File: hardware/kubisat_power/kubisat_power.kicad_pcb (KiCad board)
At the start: 2 copper layers, 21 parts, among them U1 TPS79601DCQ, U2 INA3221

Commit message: complete schematic, todo add solar connectors
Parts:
- added BT1: 1048P, 1048P:BAT_1048P, F.Cu at (171.5, 88.1)
- added C10: 22u, Capacitor_SMD:C_1206_3216Metric, F.Cu at (190.2, 117.8)
- added C11: 100n, Capacitor_SMD:C_0805_2012Metric, F.Cu at (157.6, 110.3)
- added C12: 10u, Capacitor_SMD:C_0805_2012Metric, F.Cu at (157.6, 113.3)
- added C13: 100n, Capacitor_SMD:C_0805_2012Metric, F.Cu at (157.6, 116.3)
- added C14: 47/50V, Capacitor_SMD:C_Elec_6.3x5.8, F.Cu at (150.4, 112.8)
- added C15: 10u, Capacitor_SMD:C_0805_2012Metric, F.Cu at (157.6, 119.3)
- added C16: 10u/25V, Capacitor_SMD:C_1210_3225Metric, F.Cu at (190.2, 121.6)
- added C17: 220n, Capacitor_SMD:C_0805_2012Metric, F.Cu at (157.6, 122.3)
- added C9: 10u, Capacitor_SMD:C_1206_3216Metric, F.Cu at (190.2, 114.5)
- added D1: SS14, Diode_SMD:D_SMA, F.Cu at (197.8, 111.0)
- added D10: PV, LED_SMD:LED_0805_2012Metric, F.Cu at (180.0, 113.3)
- added D11: 5V_OK, LED_SMD:LED_0805_2012Metric, F.Cu at (180.0, 116.3)
- added D2: U_CHG, LED_SMD:LED_0805_2012Metric, F.Cu at (171.1, 110.3)
- added D3: U_DONE, LED_SMD:LED_0805_2012Metric, F.Cu at (171.1, 113.3)
- added D4: S_DONE, LED_SMD:LED_0805_2012Metric, F.Cu at (171.1, 116.3)
- added D5: S_CHG, LED_SMD:LED_0805_2012Metric, F.Cu at (175.6, 110.3)
- added D6: SS54, Diode_SMD:D_SMA, F.Cu at (197.8, 115.6)
- added D7: TC, LED_SMD:LED_0805_2012Metric, F.Cu at (175.6, 113.3)
- added D8: WARN, LED_SMD:LED_0805_2012Metric, F.Cu at (175.6, 116.3)
- added D9: CRIT, LED_SMD:LED_0805_2012Metric, F.Cu at (180.0, 110.3)
- added J1: USB_C_Receptacle_PowerOnly_6P, Connector_USB:USB_C_Receptacle_HRO_TYPE-C-31-M-17, F.Cu at (174.7, 122.9)
- added JP1: SolderJumper_2_Open, Jumper:SolderJumper-2_P1.3mm_Open_RoundedPad1.0x1.5mm, F.Cu at (189.5, 125.5)
- added L1: 3.3.uH, Inductor_SMD:L_Cenker_CKCS5040, F.Cu at (197.3, 121.2)
- added L2: 100, Inductor_SMD:L_Bourns_SRP7028A_7.3x6.6mm, F.Cu at (150.4, 121.0)
- added Q1: Si2305, Package_TO_SOT_SMD:SOT-23, F.Cu at (211.3, 124.4)
- added R12: 10k, Resistor_SMD:R_0805_2012Metric, F.Cu at (130.0, 110.2)
- added R13: 13k3, Resistor_SMD:R_0805_2012Metric, F.Cu at (130.0, 113.2)
- added R14: 1k5, Resistor_SMD:R_0805_2012Metric, F.Cu at (130.0, 116.1)
- added R15: 1k, Resistor_SMD:R_0805_2012Metric, F.Cu at (130.0, 119.1)
- added R16: 1k, Resistor_SMD:R_0805_2012Metric, F.Cu at (130.0, 122.0)
- added R17: 5k1, Resistor_SMD:R_0805_2012Metric, F.Cu at (130.0, 125.0)
- added R18: 5k1, Resistor_SMD:R_0805_2012Metric, F.Cu at (134.4, 110.2)
- added R19: 1k, Resistor_SMD:R_2512_6332Metric_Pad1.40x3.35mm_HandSolder, F.Cu at (164.3, 111.2)
- added R20: 100, Resistor_SMD:R_2512_6332Metric_Pad1.40x3.35mm_HandSolder, F.Cu at (164.3, 116.1)
- added R21: 27k, Resistor_SMD:R_0805_2012Metric, F.Cu at (134.4, 113.2)
- added R22: 6k8, Resistor_SMD:R_0805_2012Metric, F.Cu at (134.4, 116.1)
- added R23: 1k, Resistor_SMD:R_0805_2012Metric, F.Cu at (134.4, 119.1)
- added R24: 1k, Resistor_SMD:R_0805_2012Metric, F.Cu at (134.4, 122.0)
- added R25: R050, Resistor_SMD:R_2512_6332Metric_Pad1.40x3.35mm_HandSolder, F.Cu at (164.3, 121.0)
- added R26: 120, Resistor_SMD:R_0805_2012Metric, F.Cu at (134.4, 125.0)
- added R27: 10k, Resistor_SMD:R_0805_2012Metric, F.Cu at (138.8, 110.2)
- added R28: 10k, Resistor_SMD:R_0805_2012Metric, F.Cu at (138.8, 113.2)
- added R29: 10k, Resistor_SMD:R_0805_2012Metric, F.Cu at (138.8, 116.1)
- added R30: 10k, Resistor_SMD:R_0805_2012Metric, F.Cu at (138.8, 119.1)
- added R31: 10k, Resistor_SMD:R_0805_2012Metric, F.Cu at (138.8, 122.0)
- added R32: 10k, Resistor_SMD:R_0805_2012Metric, F.Cu at (138.8, 125.0)
- added R33: 1k, Resistor_SMD:R_0805_2012Metric, F.Cu at (143.2, 110.2)
- added R34: 1k, Resistor_SMD:R_0805_2012Metric, F.Cu at (143.2, 113.2)
- added R35: 1k, Resistor_SMD:R_0805_2012Metric, F.Cu at (143.2, 116.1)
- added R36: 1k, Resistor_SMD:R_0805_2012Metric, F.Cu at (143.2, 119.1)
- added R37: 1k, Resistor_SMD:R_0805_2012Metric, F.Cu at (143.2, 122.0)
- added SW1: SW_Wuerth_450301014042, Button_Switch_THT:SW_Slide-03_Wuerth-WS-SLTV_10x2.5x6.4_P2.54mm, F.Cu at (188.0, 110.8)
- added U3: LN2220, Package_TO_SOT_SMD:TSOT-23-6_HandSoldering, F.Cu at (205.3, 124.3)
- added U4: CN3791, Package_SO:SSOP-10-1EP_3.9x4.9mm_P1mm_EP2.1x3.3mm, F.Cu at (206.1, 112.2)
- added U5: TP4056, Package_SO:SOIC-8-1EP_3.9x4.9mm_P1.27mm_EP2.29x3mm, F.Cu at (206.1, 118.8)
- added U6: DW01A, Package_TO_SOT_SMD:SOT-23-6, F.Cu at (184.8, 115.2)
- added U7: FS8205, Package_TO_SOT_SMD:SOT-23-6, F.Cu at (184.8, 119.8)
- R11, R5, R8: value 0R1 -> 0R01
- moved C1 128.5 mm to (153.2, 143.6)
- moved C4 128.5 mm to (146.2, 168.6)
- moved R2 128.5 mm to (155.7, 138.7)
- moved R8 128.5 mm to (146.1, 160.6)
- moved U2 128.5 mm to (145.7, 174.0)
- moved C2 128.5 mm to (161.8, 137.2)
- moved C3 128.5 mm to (151.6, 171.1)
- moved C5 128.5 mm to (138.6, 173.0)
- moved C6 128.5 mm to (141.6, 176.6)
- moved C7 128.5 mm to (161.8, 143.0)
- moved C8 128.5 mm to (161.8, 148.9)
- moved R1 128.5 mm to (155.7, 135.7)
- moved R10 128.5 mm to (134.7, 171.6)
- moved R11 128.5 mm to (129.1, 173.5)
- moved R3 128.5 mm to (154.7, 169.1)
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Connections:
- net 3V3 renamed +3V3
- net DRAW_SENSE_H renamed 5V_SENSE_IN
- net SOLAR_SENSE_H renamed SOLAR_SENSE_IN
- net USB_SENSE_H renamed USB_SENSE_IN
- C2 pad 1: REG_IN -> 5V_SENSE_OUT
- C6 pad 1: GND -> 5V_SENSE_OUT
- C6 pad 2: Net-(U2-VS) -> GND
- C7 pad 1: Net-(U2-VS) -> 5V_SENSE_OUT
- R10 pad 1: DRAW_SENSE_L -> 5V_SENSE_OUT
- R11 pad 2: DRAW_SENSE_L -> 5V_SENSE_OUT
- R4 pad 1: SOLAR_sENSE_L -> SOLAR_SENSE_OUT
- R5 pad 2: SOLAR_sENSE_L -> SOLAR_SENSE_OUT
- R7 pad 1: USB_SENSE_L -> SOLAR_SENSE_OUT
- R8 pad 1: USB_SENSE_L -> SOLAR_SENSE_OUT
- U1 pad 2: REG_IN -> 5V_SENSE_OUT
- U2 pad 10: unconnected-(U2-PV-Pad10) -> Net-(D10-K)
- U2 pad 13: unconnected-(U2-TC-Pad13) -> Net-(D7-K)
- U2 pad 16: unconnected-(U2-VPU-Pad16) -> 5V_SENSE_OUT
- U2 pad 4: Net-(U2-VS) -> 5V_SENSE_OUT
- U2 pad 6: VSENSE_SCL -> INA3221_SCL
- U2 pad 7: VSENSE_SDA -> INA3221_SDA
- U2 pad 8: unconnected-(U2-WARNING-Pad8) -> Net-(D8-K)
- U2 pad 9: unconnected-(U2-CRITICAL-Pad9) -> Net-(D9-K)
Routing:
- net SOLAR_SENSE_OUT: track 0.00 -> 9.69 mm
- net 5V_SENSE_OUT: track 0.00 -> 6.39 mm
- net DRAW_SENSE_L: track 6.39 -> 0.00 mm
- net SOLAR_sENSE_L: track 5.21 -> 0.00 mm
- net USB_SENSE_L: track 4.49 -> 0.00 mm

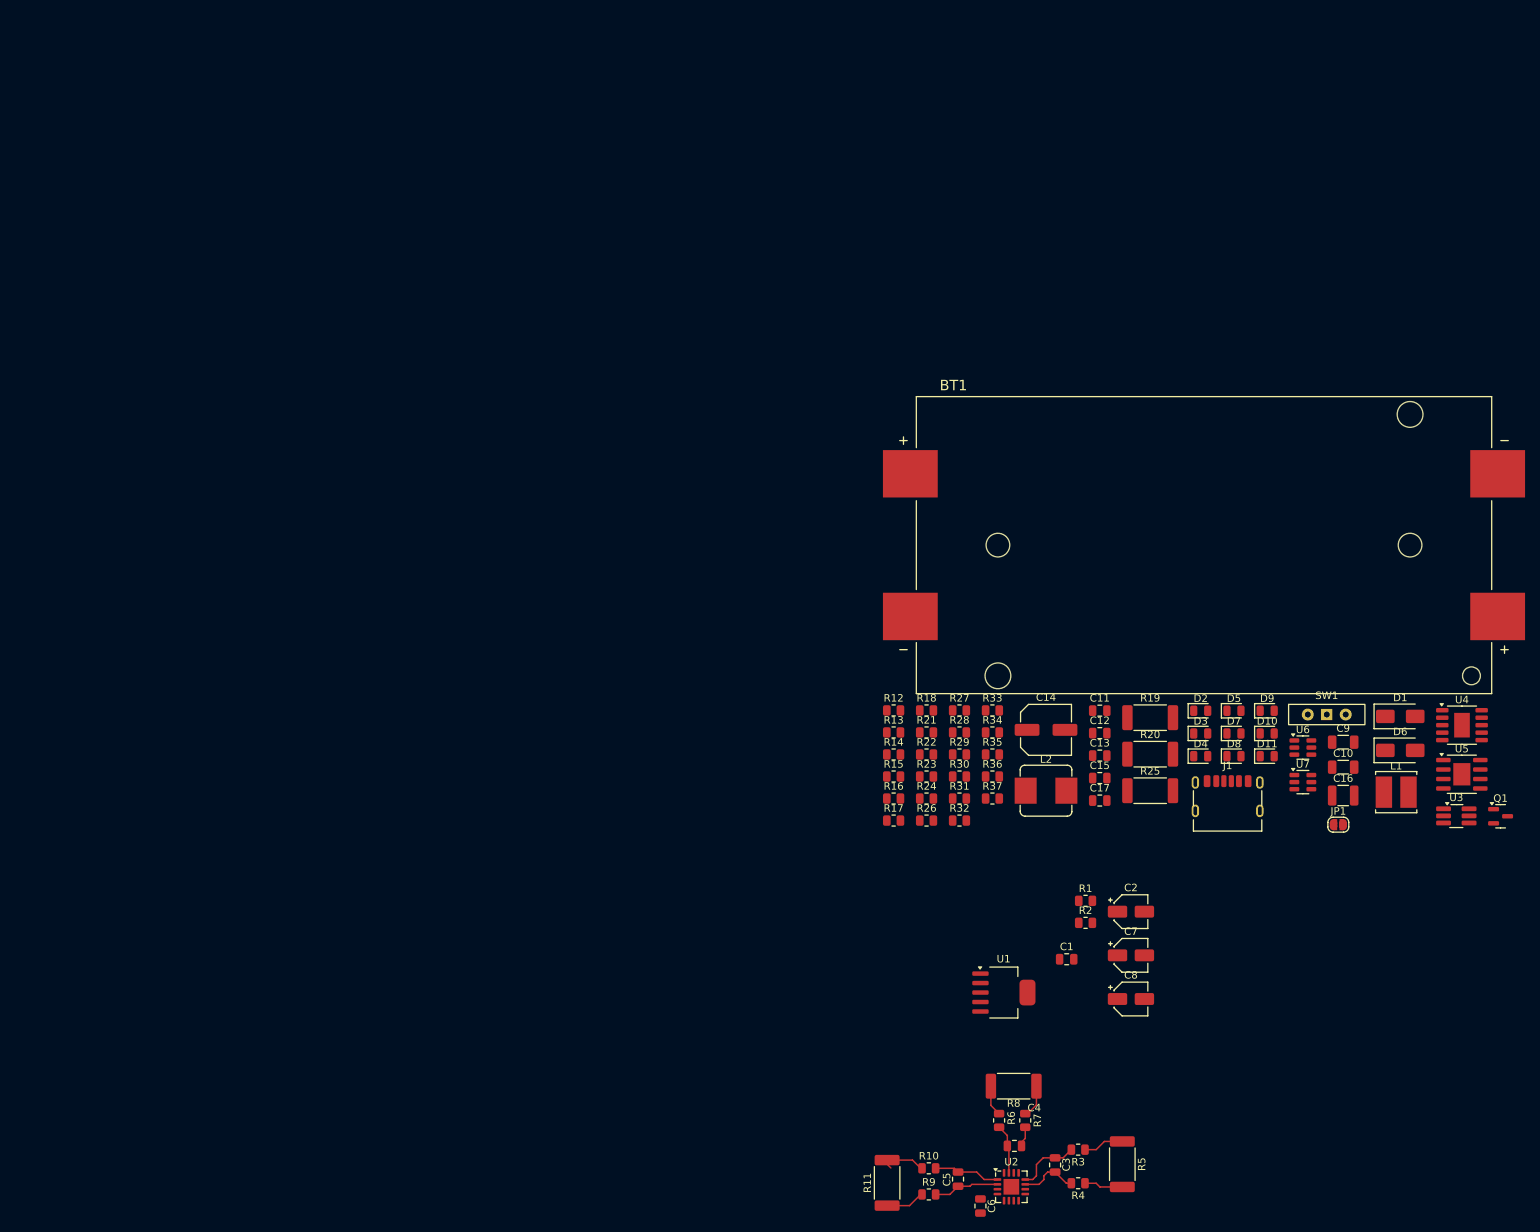
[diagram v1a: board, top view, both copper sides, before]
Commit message: changed battery holder
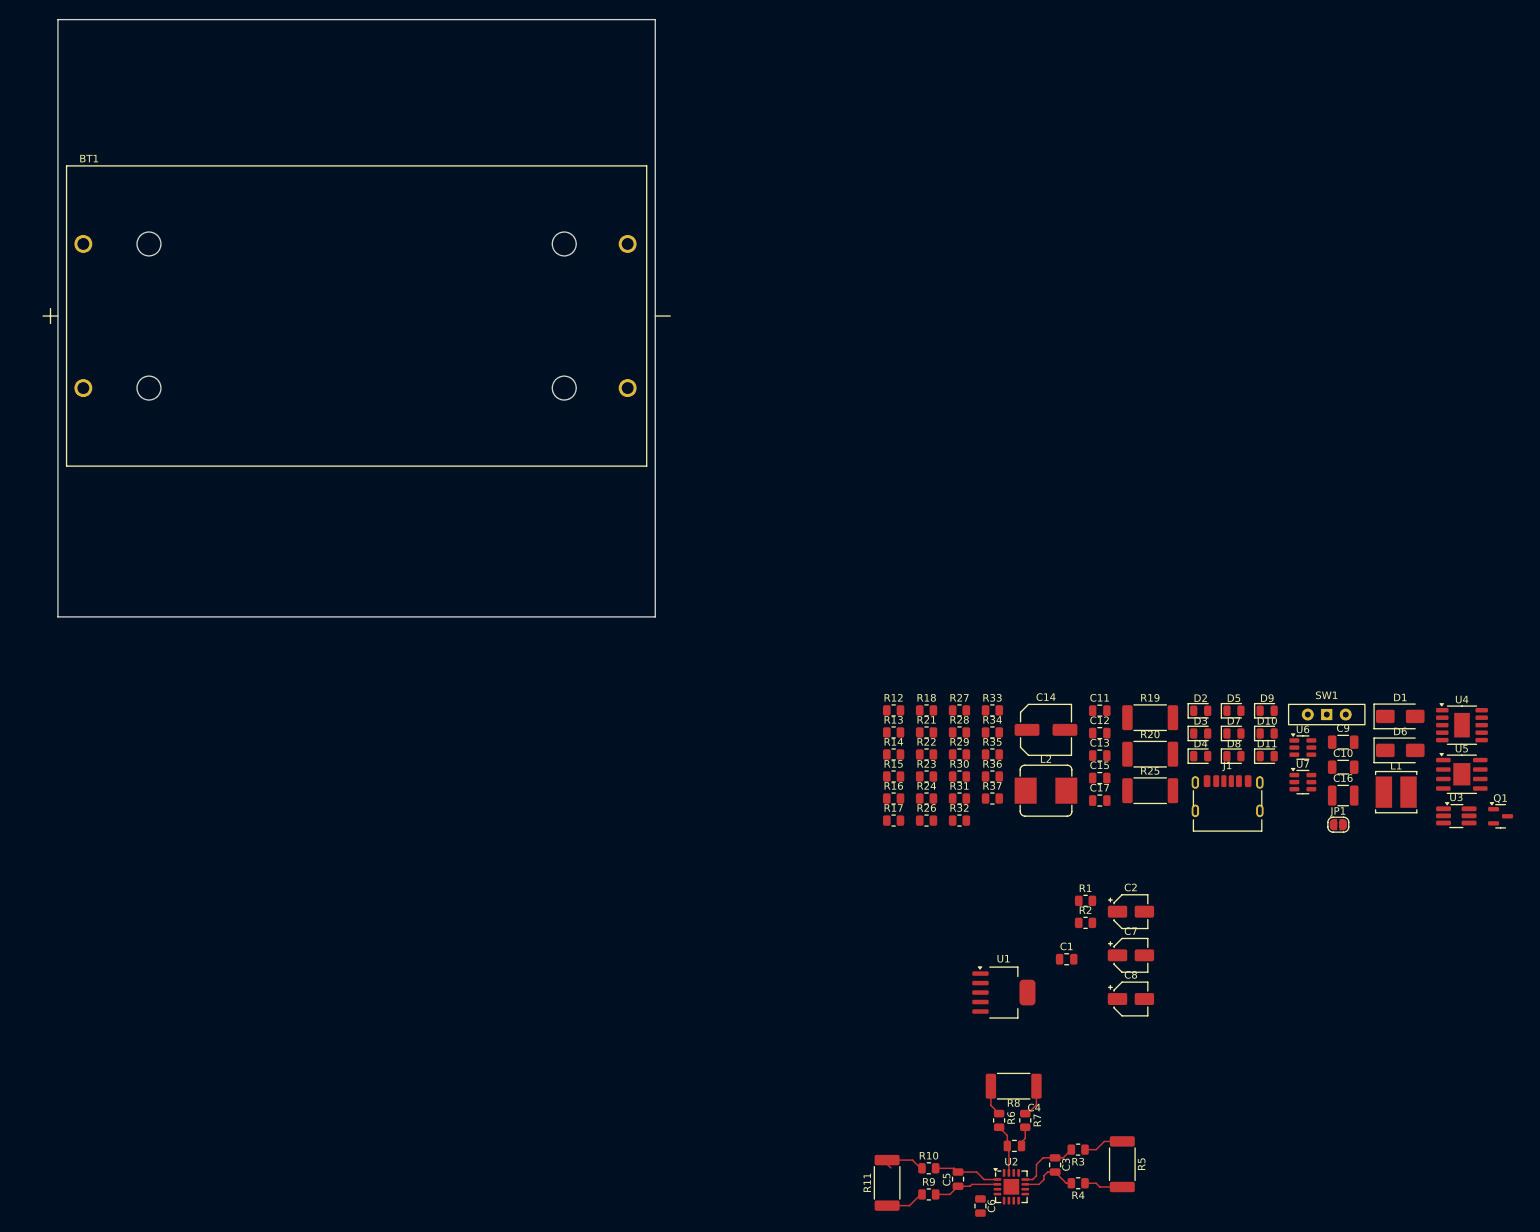
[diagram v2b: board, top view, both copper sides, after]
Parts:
- BT1: value 1048P -> BK-18650-PC4; footprint 1048P:BAT_1048P -> Library:BAT_BK-18650-PC4
- moved BT1 117.6 mm to (58.0, 57.4)
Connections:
- R20 pad 1: Net-(BT1-PadP1) -> Net-(BT1-Pad1+)
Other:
- board outline added: 80 x 80 mm

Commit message: completed schematic with solar connectors, changed 3v3 regulator
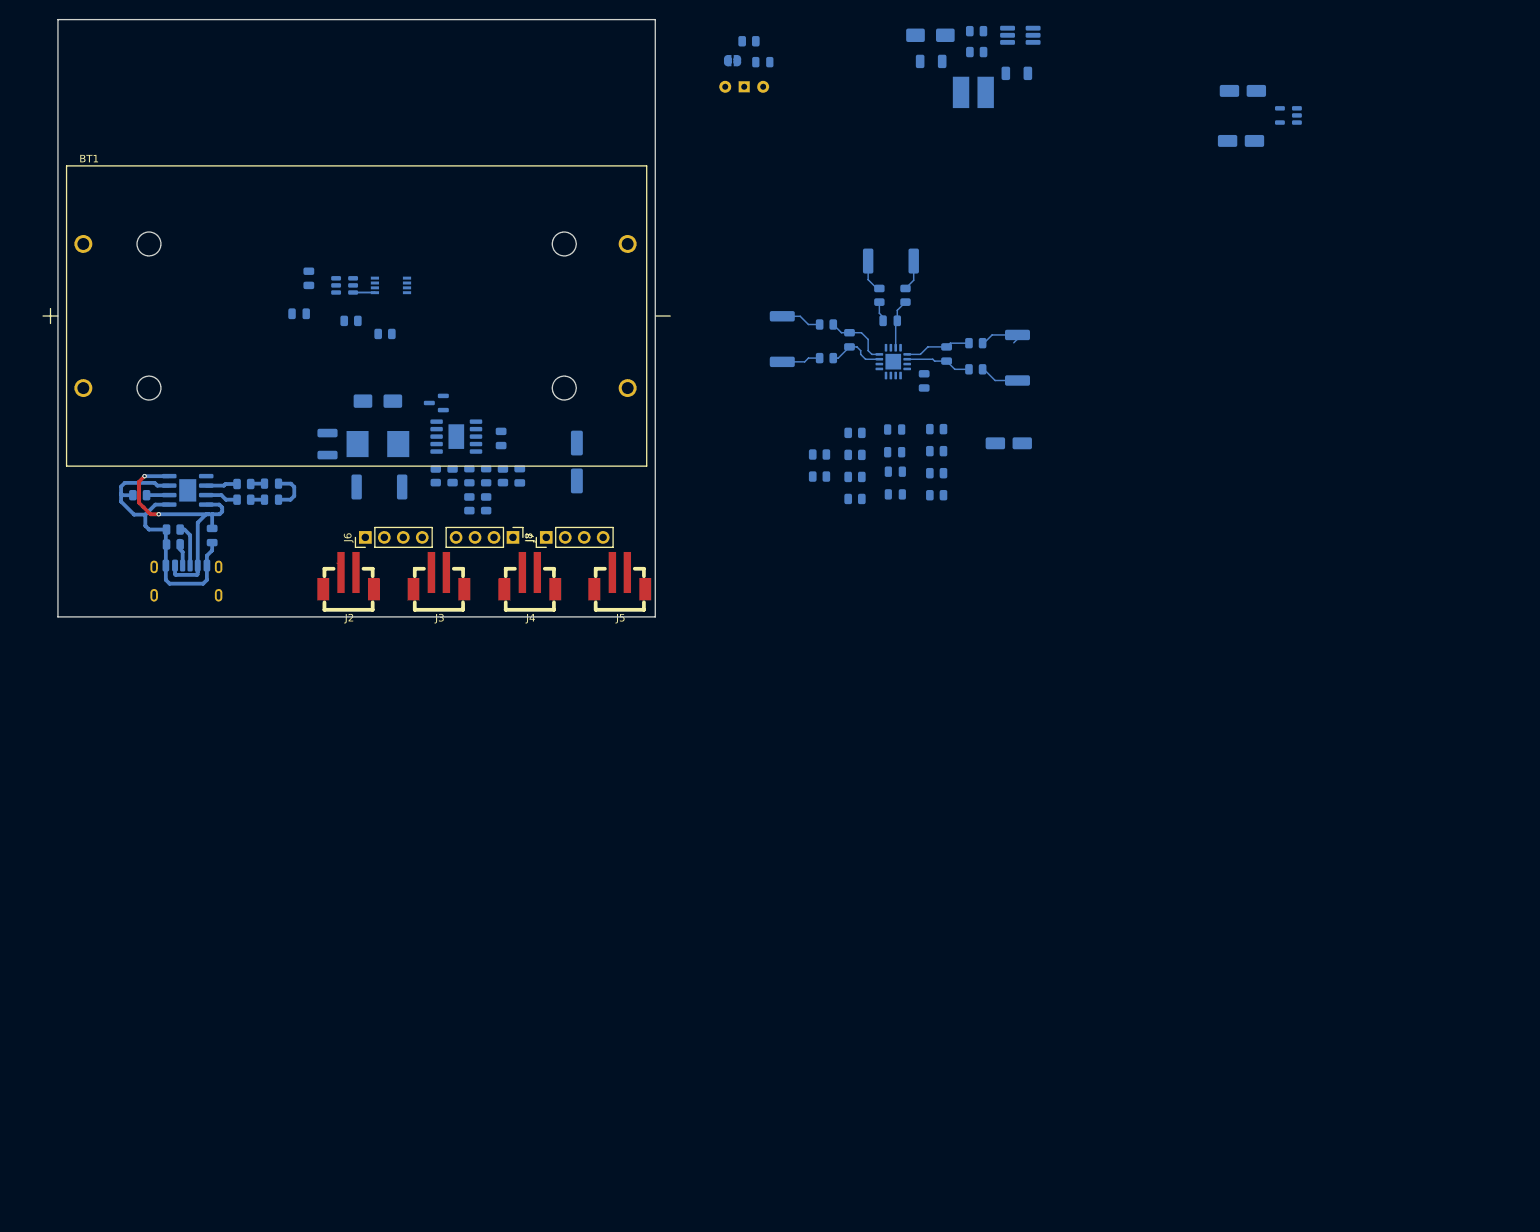
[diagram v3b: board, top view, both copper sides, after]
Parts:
- removed C1: 15p, Capacitor_SMD:C_0805_2012Metric
- removed R1: 51k, Resistor_SMD:R_0805_2012Metric
- removed R2: 30k1, Resistor_SMD:R_0805_2012Metric
- added J2: B2B-PH-SM4-TB_LF__SN_, kubisat:B2B-PH-SM4-TB_LF__SN_, F.Cu at (57.0, 91.8)
- added J3: B2B-PH-SM4-TB_LF__SN_, kubisat:B2B-PH-SM4-TB_LF__SN_, F.Cu at (69.1, 91.8)
- added J4: B2B-PH-SM4-TB_LF__SN_, kubisat:B2B-PH-SM4-TB_LF__SN_, F.Cu at (81.2, 91.8)
- added J5: B2B-PH-SM4-TB_LF__SN_, kubisat:B2B-PH-SM4-TB_LF__SN_, F.Cu at (93.3, 91.8)
- added J6: Conn_01x04_Pin, Connector_PinHeader_2.54mm:PinHeader_1x04_P2.54mm_Vertical, F.Cu at (59.2, 87.0)
- added J7: Conn_01x04_Pin, Connector_PinHeader_2.54mm:PinHeader_1x04_P2.54mm_Vertical, F.Cu at (79.0, 87.0)
- added J8: Conn_01x04_Pin, Connector_PinHeader_2.54mm:PinHeader_1x04_P2.54mm_Vertical, F.Cu at (83.5, 87.0)
- C10, C11, C12, C13, C14, C15, C16, C17, C3, C4, C5, C6, C7, C9, D1, D10, D11, D2, D3, D4, D5, D6, D7, D8, D9, J1, JP1, L1, L2, Q1, R10, R11, R12, R13, R14, R15, R16, R17, R18, R21, R22, R23, R24, R25, R26, R27, R28, R29, R3, R30, R31, R32, R33, R34, R35, R36, R37, R4, R5, R6, R7, R8, R9, SW1, U2, U3, U4, U5, U6: moved to B.Cu
- C2: value 2u2 -> 10u; moved to B.Cu
- C8: value 1u -> 10u; moved to B.Cu
- R19, R20: footprint Resistor_SMD:R_2512_6332Metric_Pad1.40x3.35mm_HandSolder -> Resistor_SMD:R_0805_2012Metric; moved to B.Cu
- U1: value TPS79601DCQ -> ~; footprint Package_TO_SOT_SMD:SOT-223-6_TabPin3 -> Package_TO_SOT_SMD:SOT-23-5; moved to B.Cu
- U7: footprint Package_TO_SOT_SMD:SOT-23-6 -> Package_SO:TSSOP-8_3x3mm_P0.65mm; moved to B.Cu
- moved U5 174.8 mm to (35.4, 80.8)
- moved Q1 152.9 mm to (68.7, 69.0), turned to 180 degrees
- moved D6 144.7 mm to (60.9, 68.8), turned to 180 degrees
- moved C16 143.9 mm to (54.1, 74.5), turned to 90 degrees
- moved U6 142.5 mm to (56.4, 53.3)
- moved J1 142.4 mm to (35.2, 94.0), turned to 180 degrees
- moved U4 140.1 mm to (71.4, 73.5), turned to 180 degrees
- moved U7 139.1 mm to (62.6, 53.3)
- moved JP1 130.6 mm to (108.4, 23.2), turned to 180 degrees
- moved D3 128.9 mm to (46.6, 79.8)
- moved D2 127.6 mm to (46.6, 82.0)
- moved C13 123.7 mm to (51.6, 52.4), turned to 90 degrees
- moved U1 123.5 mm to (182.8, 30.5), turned to 180 degrees
- moved C11 121.2 mm to (38.7, 86.8), turned to -90 degrees
- moved C12 121.1 mm to (50.4, 57.1), turned to 180 degrees
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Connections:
- BT1 pad 1+: Net-(BT1-Pad1+) -> SOLAR_SENSE_OUT
- BT1 pad 2+: Net-(BT1-Pad1+) -> SOLAR_SENSE_OUT
- C13 pad 1: SOLAR_SENSE_OUT -> Net-(U6-VCC)
- R20 pad 1: Net-(BT1-Pad1+) -> SOLAR_SENSE_OUT
- R20 pad 2: SOLAR_SENSE_OUT -> Net-(U6-VCC)
- U1 pad 1: REG_EN -> 5V_SENSE_OUT
- U1 pad 2: 5V_SENSE_OUT -> GND
- U1 pad 3: GND -> REG_EN
- U1 pad 4: +3V3 -> unconnected-(U1-NC-Pad4)
- U1 pad 5: Net-(U1-NR/FB) -> +3V3
- U6 pad 5: SOLAR_SENSE_OUT -> Net-(U6-VCC)
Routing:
- net GND: track 0.00 -> 40.9 mm
- net Net-(U5-CE): track 0.00 -> 37.0 mm, vias 0 -> 2
- net INFO_LED_ENABLE: track 0.00 -> 5.82 mm
- net Net-(J1-CC1): track 0.00 -> 5.72 mm
- net Net-(U5-~{CHRG}): track 0.00 -> 4.39 mm
- net Net-(U5-~{STDBY}): track 0.00 -> 4.22 mm
- net Net-(J1-CC2): track 0.00 -> 3.62 mm
- net Net-(U5-PROG): track 0.00 -> 3.10 mm
- net Net-(U6-GND): track 0.00 -> 2.94 mm
- net Net-(D3-K): track 0.00 -> 1.87 mm
- net Net-(D2-K): track 0.00 -> 1.85 mm
- net VS: track 0.00 -> 1.47 mm
